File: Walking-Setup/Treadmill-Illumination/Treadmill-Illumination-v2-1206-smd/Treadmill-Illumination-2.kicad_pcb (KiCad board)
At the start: 2 copper layers, 56 x 34 mm, 11 parts, among them J2 S2B-PH-SM4-TB

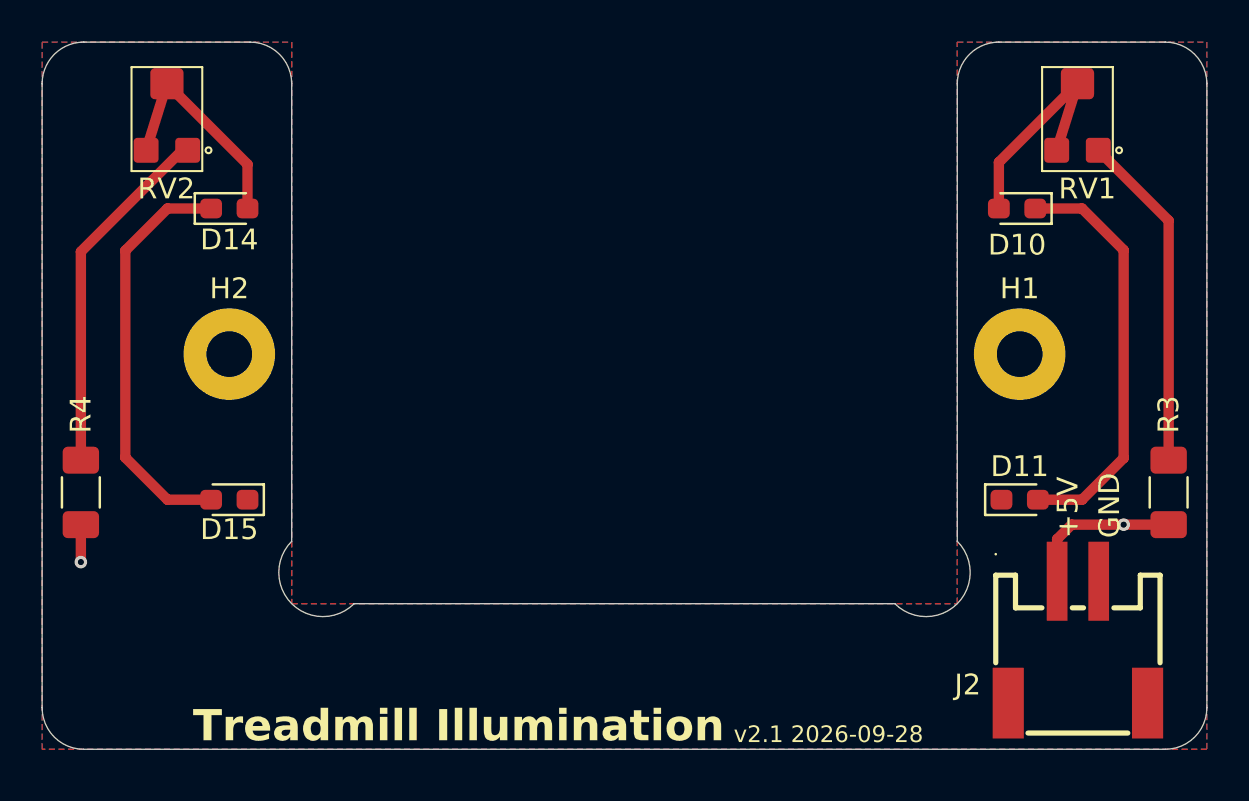
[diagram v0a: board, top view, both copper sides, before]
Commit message: Restructure Treadmill-Illumination into standalone projects with shared libraries
Rename v1/, v2/0603/ and v2/1206/ to Treadmill-Illumination-v1/,
Treadmill-Illumination-v2-0603-smd/ and
Treadmill-Illumination-v2-1206-smd/
so each project folder is identifiable on its own.

Both v2 variants carried identical copies of the EasyEDA/LCSC
connector
(C295747) and trimmer (C48997897) libraries. Keep a single copy
in
libraries/ and point the lib tables, footprint 3D model paths and
board
model paths to ${KIPRJMOD}/../libraries/.

Regenerate schematic PDF, STEP, GLB and top/bottom renders for
all three
projects into their assets/ folders, optimize PNGs, and update
the doc
page for the new paths.
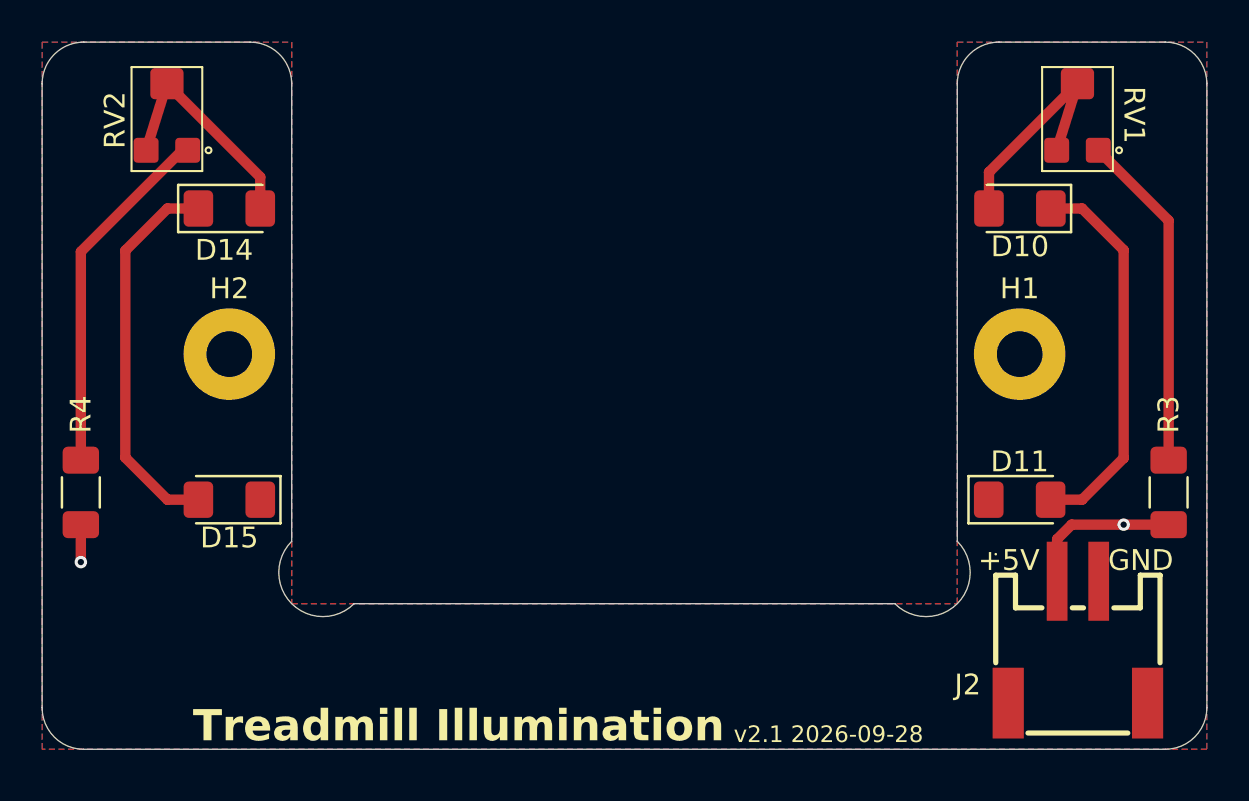
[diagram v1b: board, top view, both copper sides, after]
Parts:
- D10, D11, D14, D15: footprint LED_SMD:LED_0603_1608Metric_Pad1.05x0.95mm_HandSolder -> LED_SMD:LED_1206_3216Metric_Pad1.42x1.75mm_HandSolder
- moved D10 0.14 mm to (123.0, 96.0)
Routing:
- net Net-(D10-K): track 20.0 -> 18.7 mm
- net Net-(D14-K): track 19.9 -> 18.7 mm
